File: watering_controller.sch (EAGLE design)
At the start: 12 parts, among them IC2 7805T, J1 DCJ0202, J2 DCJ0202, Q1 IRLZ44Z

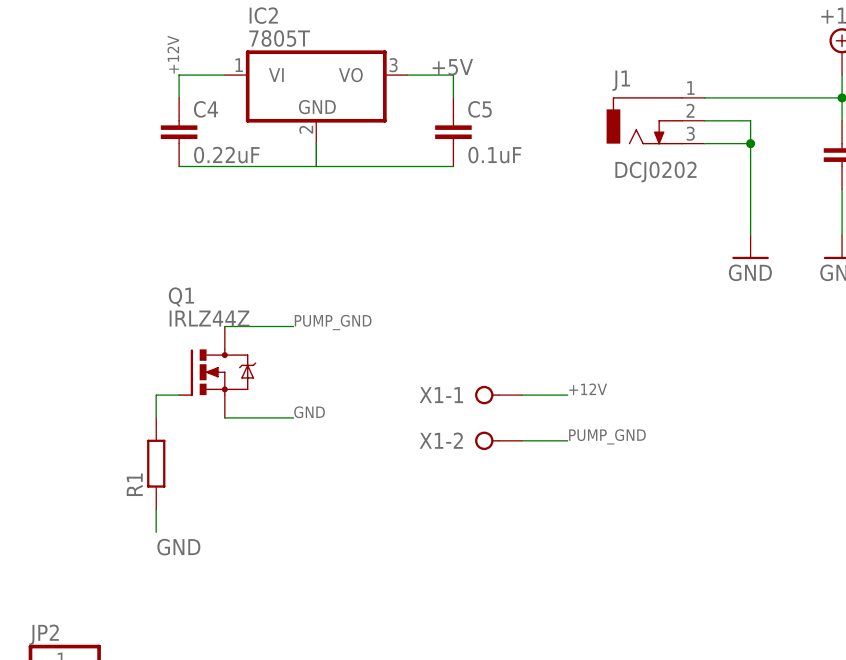
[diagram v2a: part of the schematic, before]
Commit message: Create watering indicator v2.0 for SMD
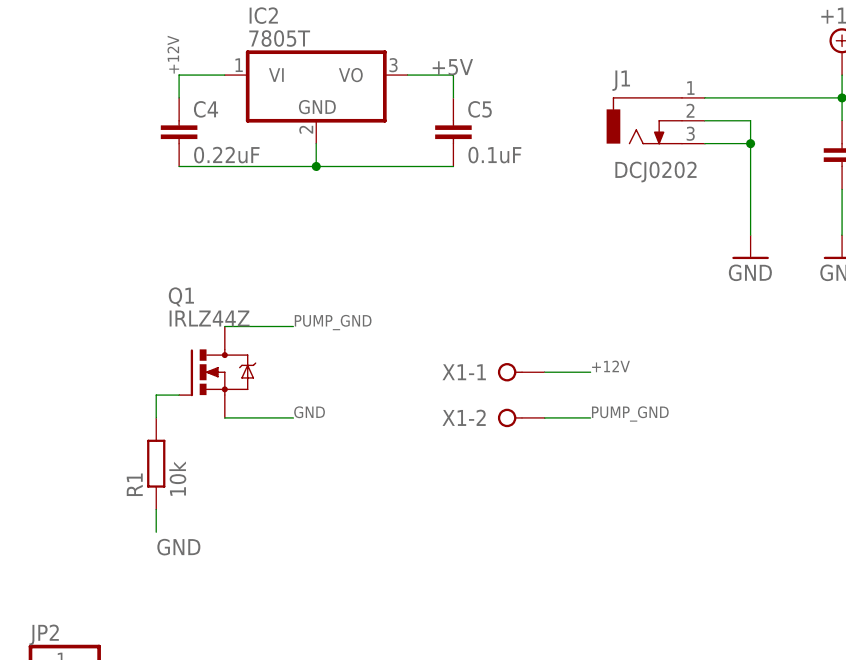
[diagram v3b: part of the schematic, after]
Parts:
- R1: value (none) -> 10k
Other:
- moved on the sheet: X1-1, X1-2
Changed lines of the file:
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@@
 <grid distance="0.1" unitdist="inch" unit="inch" style="lines" multiple="1" display="no" altdistance="0.01" altunitdist="inch" altunit="inch"/>
 <layers>
-<layer number="1" name="Top" color="4" fill="1" visible="yes" active="no"/>
-<layer number="16" name="Bottom" color="1" fill="1" visible="yes" active="no"/>
-<layer number="17" name="Pads" color="2" fill="1" visible="yes" active="no"/>
-<layer number="18" name="Vias" color="2" fill="1" visible="yes" active="no"/>
-<layer number="19" name="Unrouted" color="6" fill="1" visible="yes" active="no"/>
-<layer number="20" name="Dimension" color="15" fill="1" visible="yes" active="no"/>
-<layer number="21" name="tPlace" color="7" fill="1" visible="yes" active="no"/>
-<layer number="22" name="bPlace" color="7" fill="1" visible="yes" active="no"/>
-<layer number="23" name="tOrigins" color="15" fill="1" visible="yes" active="no"/>
-<layer number="24" name="bOrigins" color="15" fill="1" visible="yes" active="no"/>
-<layer number="25" name="tNames" color="7" fill="1" visible="yes" active="no"/>
-<layer number="26" name="bNames" color="7" fill="1" visible="yes" active="no"/>
-<layer number="27" name="tValues" color="7" fill="1" visible="yes" active="no"/>
-<layer number="28" name="bValues" color="7" fill="1" visible="yes" active="no"/>
+<layer number="1" name="Top" color="4" fill="1" visible="no" active="no"/>
+<layer number="16" name="Bottom" color="1" fill="1" visible="no" active="no"/>
+<layer number="17" name="Pads" color="2" fill="1" visible="no" active="no"/>
+<layer number="18" name="Vias" color="2" fill="1" visible="no" active="no"/>
+<layer number="19" name="Unrouted" color="6" fill="1" visible="no" active="no"/>
+<layer number="20" name="Dimension" color="15" fill="1" visible="no" active="no"/>
+<layer number="21" name="tPlace" color="7" fill="1" visible="no" active="no"/>
+<layer number="22" name="bPlace" color="7" fill="1" visible="no" active="no"/>
+<layer number="23" name="tOrigins" color="15" fill="1" visible="no" active="no"/>
+<layer number="24" name="bOrigins" color="15" fill="1" visible="no" active="no"/>
+<layer number="25" name="tNames" color="7" fill="1" visible="no" active="no"/>
+<layer number="26" name="bNames" color="7" fill="1" visible="no" active="no"/>
+<layer number="27" name="tValues" color="7" fill="1" visible="no" active="no"/>
+<layer number="28" name="bValues" color="7" fill="1" visible="no" active="no"/>
 <layer number="29" name="tStop" color="7" fill="3" visible="no" active="no"/>
 <layer number="30" name="bStop" color="7" fill="6" visible="no" active="no"/>
@@
 <layer number="35" name="tGlue" color="7" fill="4" visible="no" active="no"/>
 <layer number="36" name="bGlue" color="7" fill="5" visible="no" active="no"/>
-<layer number="37" name="tTest" color="7" fill="1" visible="yes" active="no"/>
-<layer number="38" name="bTest" color="7" fill="1" visible="yes" active="no"/>
+<layer number="37" name="tTest" color="7" fill="1" visible="no" active="no"/>
+<layer number="38" name="bTest" color="7" fill="1" visible="no" active="no"/>
 <layer number="39" name="tKeepout" color="4" fill="11" visible="no" active="no"/>
 <layer number="40" name="bKeepout" color="1" fill="11" visible="no" active="no"/>
@@
 <layer number="44" name="Drills" color="7" fill="1" visible="no" active="no"/>
 <layer number="45" name="Holes" color="7" fill="1" visible="no" active="no"/>
-<layer number="46" name="Milling" color="3" fill="1" visible="yes" active="no"/>
-<layer number="47" name="Measures" color="7" fill="1" visible="yes" active="no"/>
-<layer number="48" name="Document" color="7" fill="1" visible="yes" active="no"/>
-<layer number="49" name="Reference" color="7" fill="1" visible="yes" active="no"/>
-<layer number="51" name="tDocu" color="7" fill="1" visible="yes" active="no"/>
-<layer number="52" name="bDocu" color="7" fill="1" visible="yes" active="no"/>
+<layer number="46" name="Milling" color="3" fill="1" visible="no" active="no"/>
+<layer number="47" name="Measures" color="7" fill="1" visible="no" active="no"/>
+<layer number="48" name="Document" color="7" fill="1" visible="no" active="no"/>
+<layer number="49" name="Reference" color="7" fill="1" visible="no" active="no"/>
+<layer number="51" name="tDocu" color="7" fill="1" visible="no" active="no"/>
+<layer number="52" name="bDocu" color="7" fill="1" visible="no" active="no"/>
 <layer number="90" name="Modules" color="5" fill="1" visible="yes" active="yes"/>
 <layer number="91" name="Nets" color="2" fill="1" visible="yes" active="yes"/>
@@
 <part name="Q1" library="transistor-power" deviceset="IRLZ44Z" device=""/>
 <part name="JP2" library="pinhead" deviceset="PINHD-1X6" device=""/>
-<part name="R1" library="resistor" deviceset="R-EU_" device="0204/5"/>
+<part name="R1" library="resistor" deviceset="R-EU_" device="0204/5" value="10k"/>
 <part name="P+2" library="supply2" deviceset="+5V" device=""/>
 <part name="GND3" library="supply1" deviceset="GND" device=""/>
@@
 <attribute name="VALUE" x="-20.32" y="44.45" size="1.778" layer="96" rot="R90"/>
 </instance>
-<instance part="X1" gate="-1" x="43.18" y="86.36"/>
-<instance part="X1" gate="-2" x="43.18" y="81.28"/>
+<instance part="X1" gate="-1" x="45.72" y="88.9"/>
+<instance part="X1" gate="-2" x="45.72" y="83.82"/>
 <instance part="Q1" gate="G$1" x="12.7" y="88.9" smashed="yes">
 <attribute name="VALUE" x="8.89" y="93.98" size="1.778" layer="96"/>
@@
 <pinref part="C5" gate="G$1" pin="2"/>
 <pinref part="C4" gate="G$1" pin="2"/>
+<junction x="25.4" y="111.76"/>
 </segment>
 </net>
@@
 <segment>
 <pinref part="X1" gate="-1" pin="KL"/>
-<wire x1="48.26" y1="86.36" x2="53.34" y2="86.36" width="0.1524" layer="91"/>
-<label x="53.34" y="86.36" size="1.27" layer="95"/>
+<wire x1="50.8" y1="88.9" x2="55.88" y2="88.9" width="0.1524" layer="91"/>
+<label x="55.88" y="88.9" size="1.27" layer="95"/>
 </segment>
 </net>
@@
 <segment>
 <pinref part="X1" gate="-2" pin="KL"/>
-<wire x1="48.26" y1="81.28" x2="53.34" y2="81.28" width="0.1524" layer="91"/>
-<label x="53.34" y="81.28" size="1.27" layer="95"/>
-</segment>
-<segment>
+<wire x1="50.8" y1="83.82" x2="55.88" y2="83.82" width="0.1524" layer="91"/>
+<label x="55.88" y="83.82" size="1.27" layer="95"/>
+</segment>
+<segment>

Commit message: Update smd version
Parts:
- removed IC2: 7805T, linear:7805T
- removed J1, J2: DCJ0202, con-jack:DCJ0202
- removed JP2: (no value), pinhead:PINHD-1X6
- removed X1: (no value), con-wago-508:W237-02P
- added 12V_J, 5V_J, PUMP_J: DCJ0202, con-jack:DCJ0202
- added C2: 0.1uF, rcl:C-EUC0805
- added IC1: NE555D, linear:NE555D
- added LED1: GREEN, led:LEDSML0805
- added MOS1: (no value), ckr_parts:FDN359BN
- added Q2, Q3: BSS123, transistor-small-signal:BSS123
- added R2: 200, resistor:R-EU_M0805
- added R3: 10k, resistor:R-EU_M0805
- added R4: 1M, pot:TRIM_EU-B25P
- C1, C3: device rcl:C-EU025-025X050 -> rcl:C-EUC0805
- C4: value 0.22uF -> 47uF; device rcl:C-EU025-025X050 -> rcl:CPOL-EUA/3216-18R
- C5: value 0.1uF -> 0.1nF; device rcl:C-EU025-025X050 -> rcl:C-EUC0805
- Q1: value IRLZ44Z -> BSS123; device transistor-power:IRLZ44Z -> transistor-small-signal:BSS123
- R1: device resistor:R-EU_0204/5 -> resistor:R-EU_M0805
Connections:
- removed net +12V: C4.1, IC2.VI, X1-1.KL
- removed net 32K: JP2.1
- removed net GND1: C4.2, C5.2, IC2.GND
- removed net SCL: JP2.3
- removed net SDA: JP2.4
- removed net SQW: JP2.2
- new net N$2: R3.2, R4.A, R4.S
- new net N$3: C4.+, IC1.DIS, IC1.THR, R3.1
- new net N$4: LED1.A, R2.1
- new net PUMP: IC1.Q, MOS1.G, R1.2
- net +5V: now also IC1.R, IC1.V+, R2.2, R4.E; no longer C5.1, IC2.VO, JP2.5
- net +9V: now also 12V_J.1, 5V_J.1, C2.1, PUMP_J.1; no longer J1.1, J2.1
- net GND: now also 12V_J.2, 12V_J.3, 5V_J.2, 5V_J.3, C4.-, C5.1, IC1.GND, LED1.C, MOS1.S; no longer J1.2, J1.3, J2.2, J2.3, JP2.6, Q1.S
- net N$1: now also C5.2, IC1.CV; no longer Q1.G, R1.2
- net PUMP_GND: now also C2.2, MOS1.D, PUMP_J.2, PUMP_J.3; no longer Q1.D, X1-2.KL
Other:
- note removed: "RTC DS3231 Connector"
- moved on the sheet: C1, C3, C5, R1
